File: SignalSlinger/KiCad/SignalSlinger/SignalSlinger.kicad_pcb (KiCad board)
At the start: 2 copper layers, 100.3 x 59.1 mm, 96 parts, among them J101 Conn_01x02, J102 Conn_01x02, J103 Conn_01x02, J104 Conn_01x02, J105 Conn_01x02, J106 Conn_01x02, J107 DB9 Female, J108 Conn_01x02, J109 Conn_01x03, J201 Barrel_Jack_Switch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

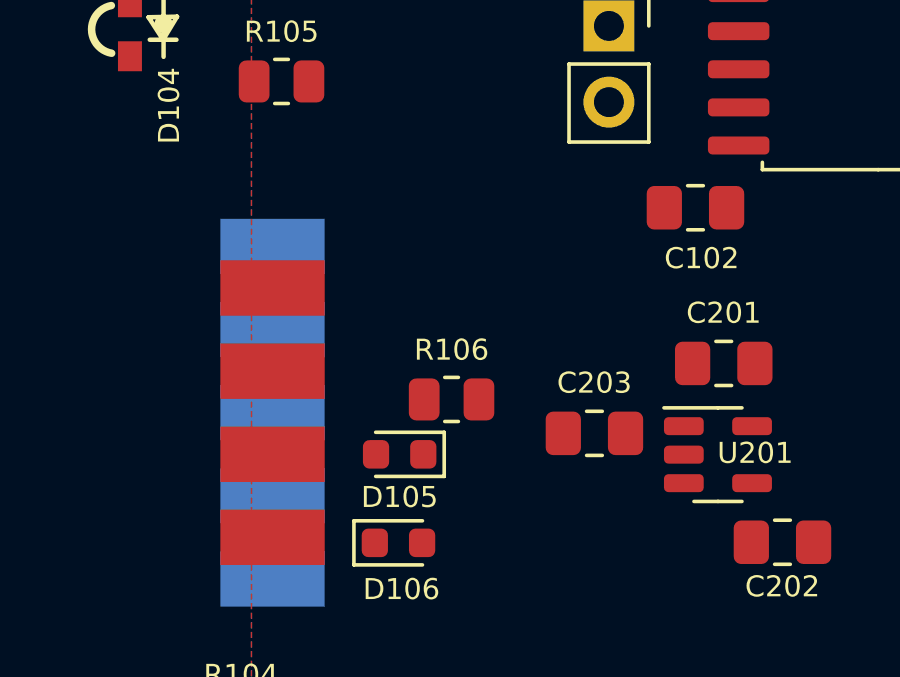
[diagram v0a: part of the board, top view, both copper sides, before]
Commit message: PCB Updates
Added parts for CW keying
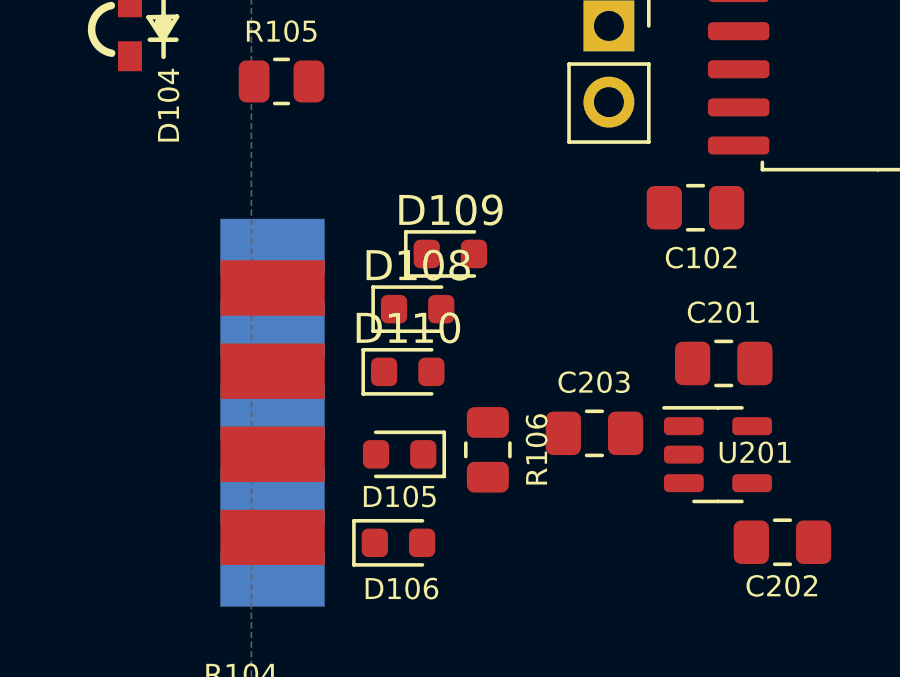
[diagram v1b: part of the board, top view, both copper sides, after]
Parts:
- added D108: ESD9B5.0ST5G_1, Diode_SMD:D_0603_1608Metric, F.Cu at (54.8, 86.0)
- added D109: ESD9B5.0ST5G_1, Diode_SMD:D_0603_1608Metric, F.Cu at (55.9, 84.1)
- added D110: ESD9B5.0ST5G_1, Diode_SMD:D_0603_1608Metric, F.Cu at (54.5, 88.0)
- D201: value BAT54C,215 -> BAT54C
- R101: value 100k -> 105k
- moved R106 2.07 mm to (57.2, 90.7), turned to -90 degrees
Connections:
- C101 pad 1: GND -> +3V3
- C101 pad 2: +3V3 -> GND
- C204 pad 1: V_ext -> GND
- C204 pad 2: GND -> V_ext
- C205 pad 1: Net-(C205-Pad1) -> GND
- C205 pad 2: GND -> Net-(C205-Pad2)
- C207 pad 1: Net-(C205-Pad1) -> GND
- C207 pad 2: GND -> Net-(C205-Pad2)
- C213 pad 1: +5V -> GND
- C213 pad 2: GND -> +5V
- C214 pad 1: +5V -> GND
- C214 pad 2: GND -> +5V
- C215 pad 1: +5V -> GND
- C215 pad 2: GND -> +5V
- D106 pad 1: Net-(D106-Pad1) -> GND
- J107 pad 1: unconnected-(J107-Pad1) -> Paddle_Dit
- J107 pad 2: unconnected-(J107-Pad2) -> Paddle Dah
- J107 pad 3: unconnected-(J107-Pad3) -> Straightkey
- J107 pad 9: Net-(D106-Pad1) -> GND
- J202 pad 2: Net-(C205-Pad1) -> Net-(C205-Pad2)
- R101 pad 1: Net-(J101-Pad1) -> Net-(D101-Pad2)
- R101 pad 2: Net-(D101-Pad2) -> Net-(J101-Pad1)
- U101 pad 1: unconnected-(U101-Pad1) -> B/B_PS_Enable
- U101 pad 2: Net-(D106-Pad1) -> GND
- U101 pad 26: unconnected-(U101-Pad26) -> Paddle_Dit
- U101 pad 27: unconnected-(U101-Pad27) -> Paddle Dah
- U101 pad 28: B/B_PS_Enable -> Straightkey
- U203 pad 2: Net-(C205-Pad1) -> Net-(C205-Pad2)

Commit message: Updates
Schematic and PCB updates
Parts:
- added R205: 105k, Resistor_SMD:R_0805_2012Metric, F.Cu at (83.1, 77.6)
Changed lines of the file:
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@@
     (property "Sheetname" "")
     (attr smd)
-    (fp_text reference "D110" (at 0 -1.43) (layer "F.SilkS")
-      (effects (font (size 1 1) (thickness 0.15)))
+    (fp_text reference "D110" (at 2.81 -0.41) (layer "F.SilkS")
+      (effects (font (size 0.7 0.7) (thickness 0.15)))
     )
     (fp_text value "ESD9B5.0ST5G_1" (at 0 1.43) (layer "F.Fab")
@@
     (property "Sheetname" "")
     (attr smd)
-    (fp_text reference "D109" (at 0 -1.43) (layer "F.SilkS")
-      (effects (font (size 1 1) (thickness 0.15)))
+    (fp_text reference "D109" (at 2.9 0.05) (layer "F.SilkS")
+      (effects (font (size 0.7 0.7) (thickness 0.15)))
     )
     (fp_text value "ESD9B5.0ST5G_1" (at 0 1.43) (layer "F.Fab")
@@
     (property "Sheetname" "")
     (attr smd)
-    (fp_text reference "R106" (at 0 -1.65 90) (layer "F.SilkS")
+    (fp_text reference "R106" (at 3.19 -0.32 90) (layer "F.SilkS")
       (effects (font (size 0.7 0.7) (thickness 0.15)))
     )
@@
       (net 19 "Net-(D101-Pad2)") (pinfunction "A") (pintype "passive"))
     (model "${KICAD6_3DMODEL_DIR}/Diode_SMD.3dshapes/D_SOD-523.wrl"
+      (offset (xyz 0 0 0))
+      (scale (xyz 1 1 1))
+      (rotate (xyz 0 0 0))
+    )
+  )
+  (footprint "Resistor_SMD:R_0805_2012Metric" (layer "F.Cu")
+    (at 83.08 77.62 180)
+    (descr "Resistor SMD 0805 (2012 Metric), square (rectangular) end terminal, IPC_7351 nominal, (Body size source: IPC-SM-782 page 72, https://www.pcb-3d.com/wordpress/wp-content/uploads/ipc-sm-782a_amendment_1_and_2.pdf), generated with kicad-footprint-generator")
+    (tags "resistor")
+    (property "Description" "RES 105K OHM 1% 1/8W 0805")
+    (property "Digi-Key Part No." "311-105KCRCT-ND")
+    (property "Link" "https://www.digikey.com/en/products/detail/yageo/RC0805FR-07105KL/727548")
+    (property "Manufacturer" "YAGEO")
+    (property "Manufacturer PN" "RC0805FR-07105KL")
+    (property "Sheetfile" "PowerSupply.kicad_sch")
+    (property "Sheetname" "Power Supply")
+    (attr smd)
+    (fp_text reference "R205" (at 0 -1.65) (layer "F.SilkS")
+      (effects (font (size 0.7 0.7) (thickness 0.15)))
+    )
+    (fp_text value "105k" (at 0 1.65) (layer "F.Fab")
+      (effects (font (size 1 1) (thickness 0.15)))
+    )
+    (fp_text user "${REFERENCE}" (at 0 0) (layer "F.Fab")
+      (effects (font (size 0.5 0.5) (thickness 0.08)))
+    )
+    (fp_line (start -0.227064 0.735) (end 0.227064 0.735) (layer "F.SilkS") (width 0.12))
+    (fp_line (start -0.227064 -0.735) (end 0.227064 -0.735) (layer "F.SilkS") (width 0.12))
+    (fp_line (start 1.68 -0.95) (end 1.68 0.95) (layer "F.CrtYd") (width 0.05))
+    (fp_line (start -1.68 0.95) (end -1.68 -0.95) (layer "F.CrtYd") (width 0.05))
+    (fp_line (start -1.68 -0.95) (end 1.68 -0.95) (layer "F.CrtYd") (width 0.05))
+    (fp_line (start 1.68 0.95) (end -1.68 0.95) (layer "F.CrtYd") (width 0.05))
+    (fp_line (start -1 0.625) (end -1 -0.625) (layer "F.Fab") (width 0.1))
+    (fp_line (start 1 -0.625) (end 1 0.625) (layer "F.Fab") (width 0.1))
+    (fp_line (start 1 0.625) (end -1 0.625) (layer "F.Fab") (width 0.1))
+    (fp_line (start -1 -0.625) (end 1 -0.625) (layer "F.Fab") (width 0.1))
+    (pad "1" smd roundrect (at -0.9125 0 180) (size 1.025 1.4) (layers "F.Cu" "F.Paste" "F.Mask") (roundrect_rratio 0.243902)
+      (net 50 "B{slash}B_PS_Enable") (pintype "passive"))
+    (pad "2" smd roundrect (at 0.9125 0 180) (size 1.025 1.4) (layers "F.Cu" "F.Paste" "F.Mask") (roundrect_rratio 0.243902)
+      (net 2 "GND") (pintype "passive"))
+    (model "${KICAD6_3DMODEL_DIR}/Resistor_SMD.3dshapes/R_0805_2012Metric.wrl"
       (offset (xyz 0 0 0))
       (scale (xyz 1 1 1))
@@
     (property "Sheetname" "")
     (attr smd)
-    (fp_text reference "D108" (at 0 -1.43) (layer "F.SilkS")
-      (effects (font (size 1 1) (thickness 0.15)))
+    (fp_text reference "D108" (at 3.01 -0.06) (layer "F.SilkS")
+      (effects (font (size 0.7 0.7) (thickness 0.15)))
     )
     (fp_text value "ESD9B5.0ST5G_1" (at 0 1.43) (layer "F.Fab")

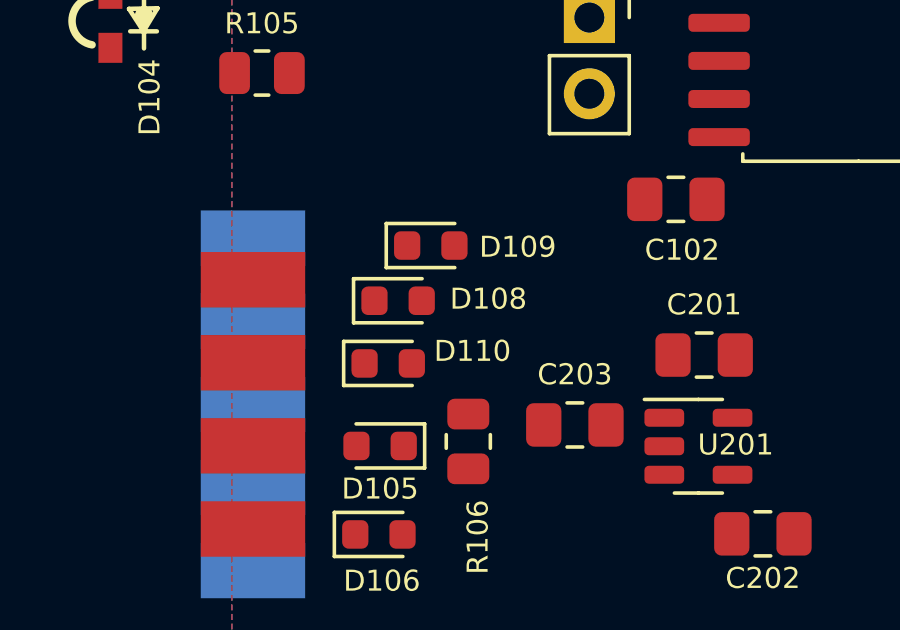
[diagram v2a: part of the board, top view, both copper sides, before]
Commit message: Schematic Debug
Fixed misplaced varistor
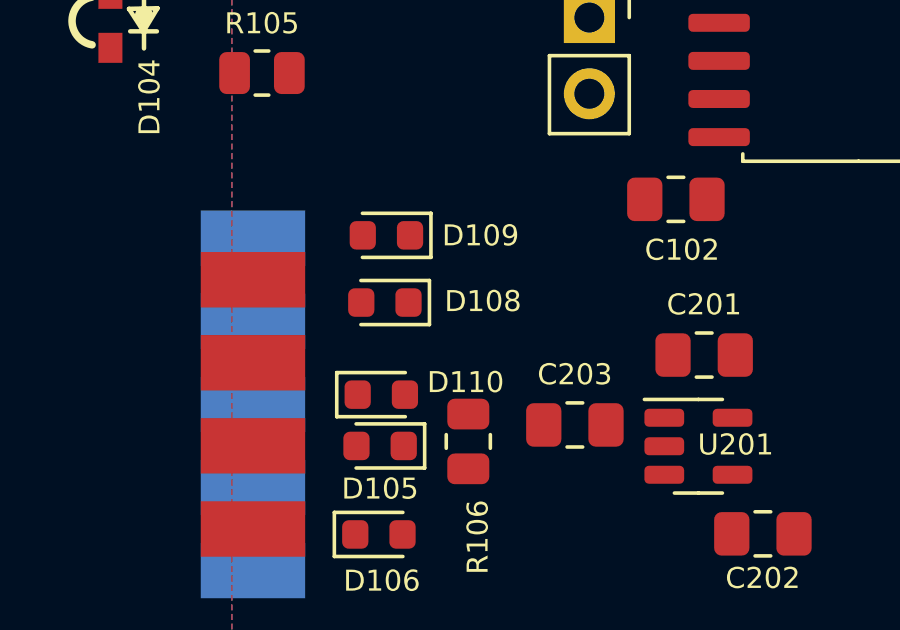
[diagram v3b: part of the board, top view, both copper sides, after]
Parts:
- moved D109 1.52 mm to (54.5, 83.8), turned to 180 degrees
- moved D110 1.07 mm to (54.3, 89.1)
- moved D108 0.44 mm to (54.4, 86.0), turned to 180 degrees
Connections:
- D108 pad 1: V+_Charging -> GND
- D108 pad 2: GND -> Paddle Dah
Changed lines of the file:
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@@
   )
   (footprint "Diode_SMD:D_0603_1608Metric" (layer "F.Cu")
-    (at 54.51 88.05)
+    (at 54.28 89.09)
     (descr "Diode SMD 0603 (1608 Metric), square (rectangular) end terminal, IPC_7351 nominal, (Body size source: http://www.tortai-tech.com/upload/download/2011102023233369053.pdf), generated with kicad-footprint-generator")
     (tags "diode")
@@
   )
   (footprint "Diode_SMD:D_0603_1608Metric" (layer "F.Cu")
-    (at 55.93 84.12)
+    (at 54.45 83.78 180)
     (descr "Diode SMD 0603 (1608 Metric), square (rectangular) end terminal, IPC_7351 nominal, (Body size source: http://www.tortai-tech.com/upload/download/2011102023233369053.pdf), generated with kicad-footprint-generator")
     (tags "diode")
@@
     (property "Sheetname" "")
     (attr smd)
-    (fp_text reference "D109" (at 2.9 0.05) (layer "F.SilkS")
+    (fp_text reference "D109" (at -3.14 -0.01) (layer "F.SilkS")
       (effects (font (size 0.7 0.7) (thickness 0.15)))
     )
@@
     (fp_line (start 0.8 -0.4) (end -0.5 -0.4) (layer "F.Fab") (width 0.1))
     (fp_line (start 0.8 0.4) (end 0.8 -0.4) (layer "F.Fab") (width 0.1))
-    (pad "1" smd roundrect (at -0.7875 0) (size 0.875 0.95) (layers "F.Cu" "F.Paste" "F.Mask") (roundrect_rratio 0.25)
+    (pad "1" smd roundrect (at -0.7875 0 180) (size 0.875 0.95) (layers "F.Cu" "F.Paste" "F.Mask") (roundrect_rratio 0.25)
       (net 2 "GND") (pinfunction "A1") (pintype "passive"))
-    (pad "2" smd roundrect (at 0.7875 0) (size 0.875 0.95) (layers "F.Cu" "F.Paste" "F.Mask") (roundrect_rratio 0.25)
+    (pad "2" smd roundrect (at 0.7875 0 180) (size 0.875 0.95) (layers "F.Cu" "F.Paste" "F.Mask") (roundrect_rratio 0.25)
       (net 51 "Paddle_Dit") (pinfunction "A2") (pintype "passive"))
     (model "${KICAD6_3DMODEL_DIR}/Diode_SMD.3dshapes/D_0603_1608Metric.wrl"
@@
   )
   (footprint "Diode_SMD:D_0603_1608Metric" (layer "F.Cu")
-    (at 54.84 85.96)
+    (at 54.4 86.02 180)
     (descr "Diode SMD 0603 (1608 Metric), square (rectangular) end terminal, IPC_7351 nominal, (Body size source: http://www.tortai-tech.com/upload/download/2011102023233369053.pdf), generated with kicad-footprint-generator")
     (tags "diode")
@@
     (property "Sheetname" "")
     (attr smd)
-    (fp_text reference "D108" (at 3.01 -0.06) (layer "F.SilkS")
+    (fp_text reference "D108" (at -3.27 0.04) (layer "F.SilkS")
       (effects (font (size 0.7 0.7) (thickness 0.15)))
     )
@@
     (fp_line (start 0.8 -0.4) (end -0.5 -0.4) (layer "F.Fab") (width 0.1))
     (fp_line (start 0.8 0.4) (end 0.8 -0.4) (layer "F.Fab") (width 0.1))
-    (pad "1" smd roundrect (at -0.7875 0) (size 0.875 0.95) (layers "F.Cu" "F.Paste" "F.Mask") (roundrect_rratio 0.25)
-      (net 30 "V+_Charging") (pinfunction "A1") (pintype "passive"))
-    (pad "2" smd roundrect (at 0.7875 0) (size 0.875 0.95) (layers "F.Cu" "F.Paste" "F.Mask") (roundrect_rratio 0.25)
-      (net 2 "GND") (pinfunction "A2") (pintype "passive"))
+    (pad "1" smd roundrect (at -0.7875 0 180) (size 0.875 0.95) (layers "F.Cu" "F.Paste" "F.Mask") (roundrect_rratio 0.25)
+      (net 2 "GND") (pinfunction "A1") (pintype "passive"))
+    (pad "2" smd roundrect (at 0.7875 0 180) (size 0.875 0.95) (layers "F.Cu" "F.Paste" "F.Mask") (roundrect_rratio 0.25)
+      (net 68 "Paddle Dah") (pinfunction "A2") (pintype "passive"))
     (model "${KICAD6_3DMODEL_DIR}/Diode_SMD.3dshapes/D_0603_1608Metric.wrl"
       (offset (xyz 0 0 0))

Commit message: Schematic
Corrected another varistor placement error.
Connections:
- D106 pad 1: GND -> Net-(D106-Pad1)
- J107 pad 9: GND -> Net-(D106-Pad1)
- U101 pad 2: GND -> Net-(D106-Pad1)
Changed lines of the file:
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@@
   (net 73 "unconnected-(U103-Pad5)")
   (net 74 "Net-(J108-Pad2)")
+  (net 75 "Net-(D106-Pad1)")
   (footprint "Connector_PinSocket_2.54mm:PinSocket_1x02_P2.54mm_Vertical" (layer "F.Cu")
     (at 43.26 107.805 90)
@@
     (fp_line (start 0.8 -0.4) (end -0.5 -0.4) (layer "F.Fab") (width 0.1))
     (pad "1" smd roundrect (at -0.7875 0) (size 0.875 0.95) (layers "F.Cu" "F.Paste" "F.Mask") (roundrect_rratio 0.25)
-      (net 2 "GND") (pinfunction "A1") (pintype "passive"))
+      (net 75 "Net-(D106-Pad1)") (pinfunction "A1") (pintype "passive"))
     (pad "2" smd roundrect (at 0.7875 0) (size 0.875 0.95) (layers "F.Cu" "F.Paste" "F.Mask") (roundrect_rratio 0.25)
       (net 2 "GND") (pinfunction "A2") (pintype "passive"))
@@
       (net 50 "B{slash}B_PS_Enable") (pinfunction "PA7") (pintype "bidirectional"))
     (pad "2" smd roundrect (at -4.65 -6.985) (size 2.05 0.6) (layers "F.Cu" "F.Paste" "F.Mask") (roundrect_rratio 0.25)
-      (net 2 "GND") (pinfunction "PC0/TxD1") (pintype "bidirectional"))
+      (net 75 "Net-(D106-Pad1)") (pinfunction "PC0/TxD1") (pintype "bidirectional"))
     (pad "3" smd roundrect (at -4.65 -5.715) (size 2.05 0.6) (layers "F.Cu" "F.Paste" "F.Mask") (roundrect_rratio 0.25)
       (net 22 "Net-(D105-Pad2)") (pinfunction "PC1/RxD1") (pintype "bidirectional"))
@@
       (net 22 "Net-(D105-Pad2)") (pinfunction "8") (pintype "passive"))
     (pad "9" smd rect locked (at -4.155 0 90) (size 1.846667 3.48) (layers "F.Cu" "F.Paste" "F.Mask")
-      (net 2 "GND") (pinfunction "9") (pintype "passive"))
+      (net 75 "Net-(D106-Pad1)") (pinfunction "9") (pintype "passive"))
     (model "${KICAD6_3DMODEL_DIR}/Connector_Dsub.3dshapes/DSUB-9_Female_EdgeMount_P2.77mm.wrl"
       (offset (xyz 0 0 0))

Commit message: PCB Development
Updates
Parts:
- moved C101 24.1 mm to (60.3, 65.2), turned to 0 degrees
- moved J102 23.5 mm to (57.8, 75.6), turned to 90 degrees
- moved C102 21.3 mm to (74.5, 64.0), turned to 180 degrees
- moved X101 20.5 mm to (61.2, 66.9), turned to 90 degrees
- moved C103 17.8 mm to (60.4, 72.6), turned to 0 degrees
- moved J105 16.8 mm to (76.9, 70.4), turned to 180 degrees
- moved U101 2.73 mm to (68.4, 74.3), turned to 180 degrees
- moved W103 1.40 mm to (96.8, 108.3)
- moved J108 1.02 mm to (91.4, 110.8)
- moved R201 0.88 mm to (88.1, 81.3)
- moved R204 0.14 mm to (94.2, 74.2)
- moved U104 0.14 mm to (95.6, 104.5)
- moved L202 0.12 mm to (89.4, 72.4)
- turned C213 to 90 degrees
- turned C214 to 90 degrees
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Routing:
- net GND: track 0.00 -> 23.5 mm, vias 0 -> 18
- net Net-(C211-Pad1): track 0.00 -> 9.23 mm
- net Net-(C208-Pad1): track 0.00 -> 2.23 mm
- added copper zone on F.Cu, net +5V
- added copper zone on F.Cu, net Net-(L202-Pad1)
- added copper zone on F.Cu, net Net-(L202-Pad2)
